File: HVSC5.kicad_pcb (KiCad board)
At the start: 2 copper layers, 220 x 152 mm, 339 parts, among them J1 test, J10 CONN_01X03, J11 test, J12 test, J13 test, J14 test, J15 test, J16 test, J17 CONN_COAXIAL, J18 CONN_01X03, J19 CONN_01X03, J2 test, J20 CONN_01X08, J21 test, J22 test, J23 test, J24 test, J25 CONN_01X05, J26 test, J27 test, J3 test, J4 test, J5 CONN_01X05, J6 test, J7 CONN_01X05, J8 CONN_COAXIAL, J9 DB9_Female_MountingHoles, SW1 SW_Push, SW3 SW_DPDT_x2, U1 AD7175-8, U10 LT1118-5V, U11 FOD0721, U12 DPBW06, U13 LTC2644, U14 uA7805, U15 INA128, U16 XR2206, U17 TLP176A, U18 ANA4522, U19 AQV258, U2 ADR4520, U20 AQV258, U21 ANA4522, U3 ADR445, U4 74LS04, U5 dsPIC33EV256GM002, U6 SN75451, U7 MAX232, U8 HFBR-2412, U9 HFBR-1414, X1 P7002SCLRP, X2 P7002SCLRP, X3 P7002SCLRP, X4 P7002SCLRP, X5 P7002SCLRP, X6 P7002SCLRP, Y1 16M, Y2 8M

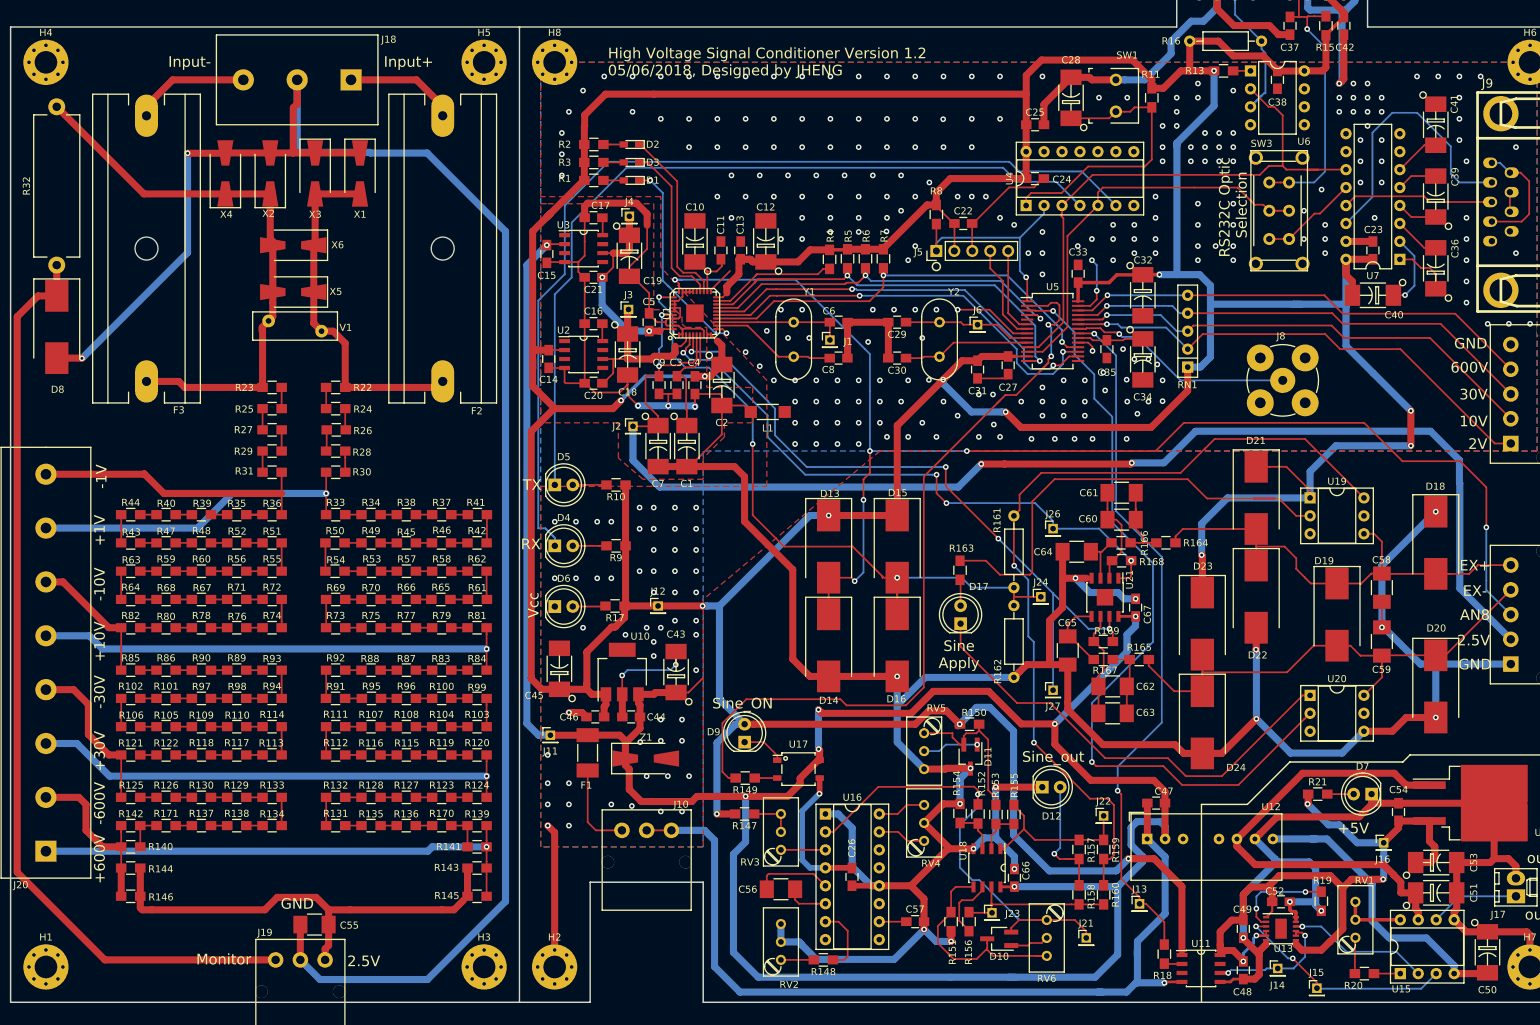
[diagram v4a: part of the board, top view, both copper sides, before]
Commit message: Selector Numbering
Selector numbering
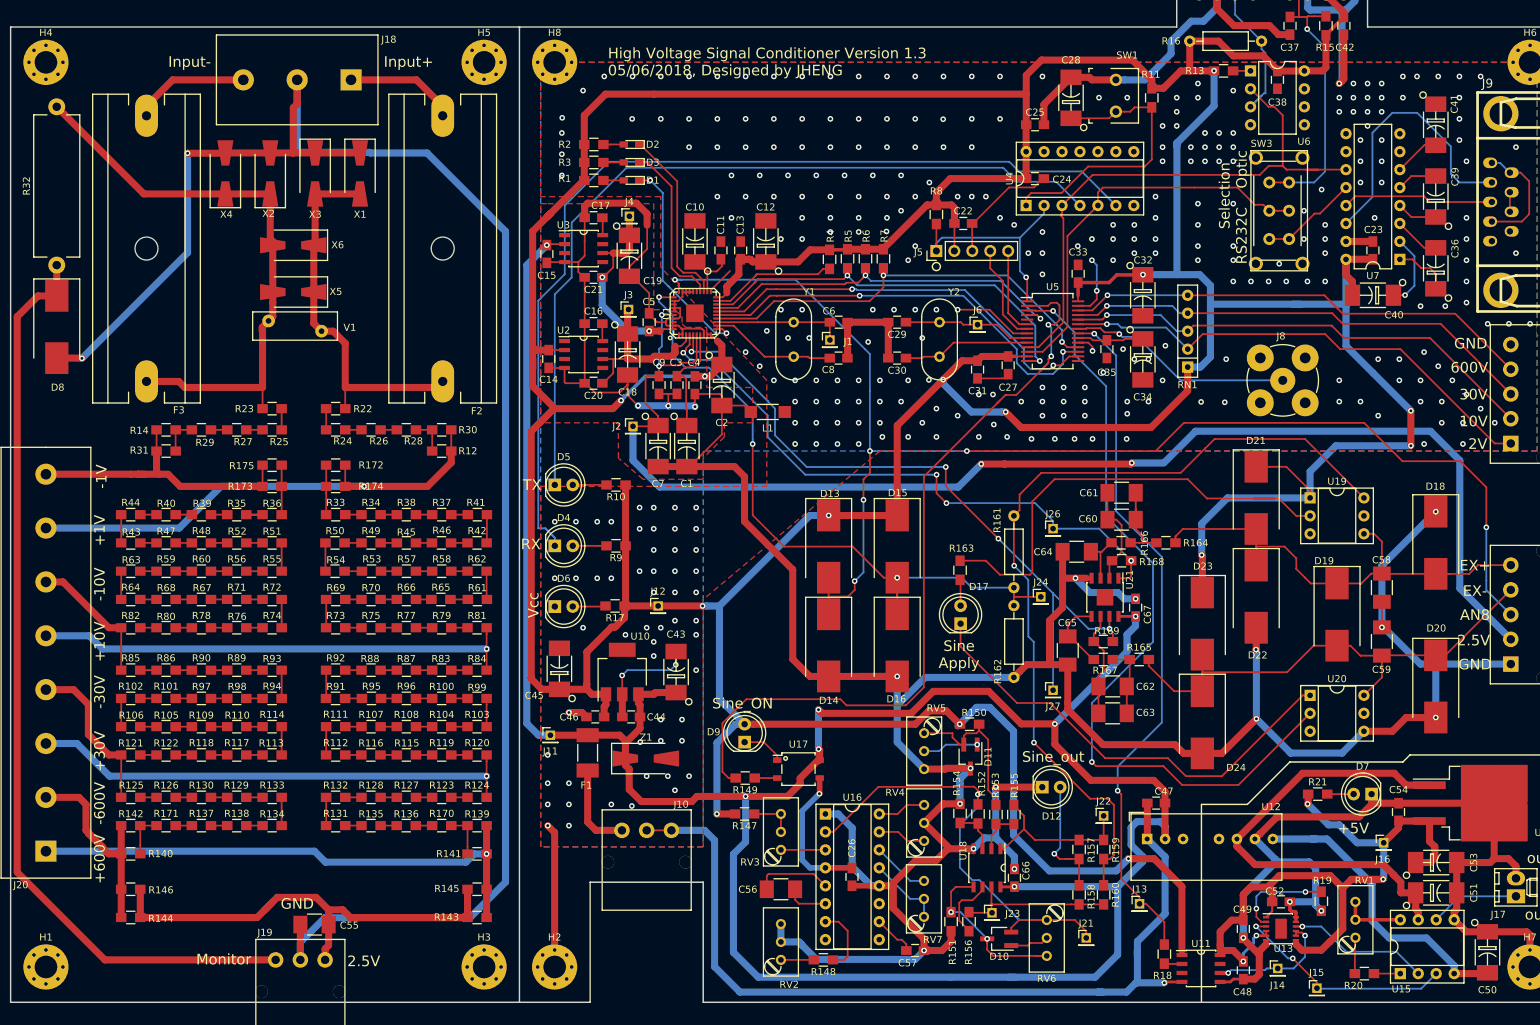
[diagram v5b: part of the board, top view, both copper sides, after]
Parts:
- added R12: 10k, Resistors_SMD:R_0805_HandSoldering, F.Cu at (104.0, 83.0)
- added R14: 10k, Resistors_SMD:R_0805_HandSoldering, F.Cu at (65.0, 80.0)
- added R172: 10k, Resistors_SMD:R_0805_HandSoldering, F.Cu at (89.0, 85.0)
- added R173: 10k, Resistors_SMD:R_0805_HandSoldering, F.Cu at (80.0, 88.0)
- added R174: 10k, Resistors_SMD:R_0805_HandSoldering, F.Cu at (89.0, 88.0)
- added R175: 10k, Resistors_SMD:R_0805_HandSoldering, F.Cu at (80.0, 85.0)
- added RV7: 500, Potentiometers:Potentiometer_Trimmer_Bourns_3296W, F.Cu at (172.2, 148.9)
- moved R30 16.2 mm to (104.0, 80.0), turned to 0 degrees
- moved R31 15.3 mm to (65.0, 83.0), turned to 180 degrees
- moved R28 10.4 mm to (99.0, 80.0)
- moved R29 10.4 mm to (70.0, 80.0)
- moved R143 7.00 mm to (109.0, 149.0)
- moved R144 7.00 mm to (60.0, 149.0)
- moved R27 5.00 mm to (75.0, 80.0), turned to 180 degrees
- moved R26 4.93 mm to (94.0, 80.0), turned to 0 degrees
- moved C57 4.08 mm to (171.0, 153.7)
- moved R22 3.00 mm to (89.0, 77.0)
- moved R23 3.00 mm to (80.0, 77.0)
- moved R24 3.00 mm to (89.0, 80.0)
- moved R25 3.00 mm to (80.0, 80.0)
- moved R140 1.00 mm to (60.0, 140.0)
- moved R141 1.00 mm to (109.0, 140.0)
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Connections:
- R33 pad 1: /Passive_Network/P1V -> Net-(R172-Pad2)
- R36 pad 1: /Passive_Network/N1V -> Net-(R173-Pad2)
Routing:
- net /Passive_Network/P1V: track 47.7 -> 71.5 mm
- net Net-(RV7-Pad1): track 0.00 -> 10.7 mm
- net /Passive_Network/P600V: track 72.6 -> 81.4 mm
- net Net-(RV7-Pad3): track 0.00 -> 8.15 mm
- net Net-(D10-Pad3): track 32.1 -> 24.7 mm, vias 0 -> 2
- net GNDREF: track 825.2 -> 818.0 mm, vias 20 -> 19
- net Net-(R173-Pad2): track 0.00 -> 7.10 mm
- net Net-(R172-Pad2): track 0.00 -> 7.00 mm
- net /Passive_Network/N600V: track 25.7 -> 32.0 mm
- net +12V: track 363.5 -> 358.8 mm
- net Net-(F1-Pad2): track 11.9 -> 15.6 mm
- net Net-(F3-Pad1): track 88.6 -> 91.6 mm
- net Net-(F2-Pad1): track 50.8 -> 53.8 mm
- net Net-(R14-Pad1): track 3.00 -> 5.30 mm
- net Net-(R12-Pad1): track 3.00 -> 5.30 mm
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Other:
- net class Power: clearance 0.2 -> 0.25
- board text added: "High Voltage Signal Conditioner Version 1.3 05/06/2018, Designed by JHENG"
- board text added: "Selection RS232C Optic"
- board text removed: "High Voltage Signal Conditioner Version 1.2 05/06/2018, Designed by JHENG"
- board text removed: "RS232C Optic Selection"

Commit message: 0805_넓히기
기타 수정
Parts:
- removed D15, D16: ES3J, Diodes_SMD:D_SMC_Handsoldering
- added C68: 20uF, Capacitors_SMD:C_1210_HandSoldering, F.Cu at (170.2, 98.0)
- added C69: 20uF, Capacitors_SMD:C_1210_HandSoldering, F.Cu at (166.6, 98.0)
- added C70: 20uF, Capacitors_SMD:C_1210_HandSoldering, F.Cu at (153.9, 96.0)
- added C71: 20uF, Capacitors_SMD:C_1210_HandSoldering, F.Cu at (170.2, 105.2)
- added C72: 20uF, Capacitors_SMD:C_1210_HandSoldering, F.Cu at (166.6, 105.2)
- added C73: 20uF, Capacitors_SMD:C_1210_HandSoldering, F.Cu at (153.9, 105.2)
- added C74: 0.1uF, Capacitors_SMD:C_0805_HandSoldering, F.Cu at (163.6, 103.6)
- added J28: test, Pin_Headers:Pin_Header_Straight_1x01_Pitch2.00mm, F.Cu at (162.6, 90.4)
- added J29: test, Pin_Headers:Pin_Header_Straight_1x01_Pitch2.00mm, F.Cu at (150.4, 90.4)
- added R176: 250, Resistors_SMD:R_0805_HandSoldering, F.Cu at (166.1, 93.7)
- added R177: 250, Resistors_SMD:R_0805_HandSoldering, F.Cu at (161.0, 93.7)
- added R178: 500, Resistors_SMD:R_0805_HandSoldering, F.Cu at (161.0, 96.3)
- added R179: 250, Resistors_SMD:R_0805_HandSoldering, F.Cu at (163.6, 110.2)
- added R180: 250, Resistors_SMD:R_0805_HandSoldering, F.Cu at (158.5, 110.2)
- added R181: 500, Resistors_SMD:R_0805_HandSoldering, F.Cu at (158.5, 107.7)
- added U22: ANA4522, USER:SOIC-8_3.9x4.9mm_Pitch1.27mm, F.Cu at (159.8, 102.6)
- D13, D14, D21, D22, D23, D24: footprint Diodes_SMD:D_SMC_Handsoldering -> USER:D_SMC_Handsoldering
- R100, R101, R102, R103, R104, R105, R106, R107, R108, R109, R110, R111, R112, R113, R114, R115, R116, R117, R118, R119, R12, R120, R121, R122, R123, R124, R125, R126, R127, R128, R129, R130, R131, R132, R133, R134, R135, R136, R137, R138, R139, R140, R141, R142, R143, R144, R145, R146, R170, R171, R172, R173, R174, R175, R22, R23, R24, R25, R26, R27, R28, R29, R30, R31, R33, R34, R35, R36, R37, R38, R39, R40, R41, R42, R43, R44, R45, R46, R47, R48, R49, R50, R51, R52, R53, R54, R55, R56, R57, R58, R59, R60, R61, R62, R63, R64, R65, R66, R67, R68, R69, R70, R71, R72, R73, R74, R75, R76, R77, R78, R79, R80, R81, R82, R83, R84, R85, R86, R87, R88, R89, R90, R91, R92, R93, R94, R95, R96, R97, R98, R99: footprint Resistors_SMD:R_0805_HandSoldering -> USER:R_0805_HandSoldering_long
- RV1: value 200 -> 2k
- U10: footprint TO_SOT_Packages_SMD:SOT-223 -> USER:SOT-223_LT1118
- U21: footprint Housings_SOIC:SOIC-8-1EP_3.9x4.9mm_Pitch1.27mm -> USER:SOIC-8_3.9x4.9mm_Pitch1.27mm
- U6: value SN75451 -> SN75452
- moved D14 97.1 mm to (255.3, 120.7), turned to 180 degrees
- moved D13 96.7 mm to (255.3, 90.4), turned to 0 degrees
- moved D6 32.2 mm to (120.0, 137.2)
- moved R17 27.1 mm to (120.7, 130.8), turned to 270 degrees
- moved J12 12.6 mm to (143.3, 114.0)
- moved C46 4.47 mm to (124.5, 116.3), turned to 90 degrees
- moved J26 2.11 mm to (192.0, 92.5)
- moved D18 0.81 mm to (243.8, 96.0)
- moved D20 0.81 mm to (243.8, 116.3)
- moved D23 0.43 mm to (211.5, 107.0)
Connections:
- C60 pad 1: Net-(C60-Pad1) -> /ADC7175/AIN2
- C61 pad 1: Net-(C60-Pad1) -> /ADC7175/AIN2
- C62 pad 1: Net-(C62-Pad1) -> /ADC7175/AIN3
- C63 pad 1: Net-(C62-Pad1) -> /ADC7175/AIN3
- D13 pad 2: /ADC7175/AIN8 -> /Voltage_Divider/Monitor
- D14 pad 1: /ADC7175/AIN8 -> /Voltage_Divider/Monitor
- J24 pad 1: /ADC7175/AIN9 -> Net-(J24-Pad1)
- J25 pad 3: /ADC7175/AIN8 -> /Voltage_Divider/Monitor
- R161 pad 1: /ADC7175/AIN9 -> Net-(J24-Pad1)
- R162 pad 2: /ADC7175/AIN9 -> Net-(J24-Pad1)
- R168 pad 2: Net-(C60-Pad1) -> Net-(R168-Pad2)
- R169 pad 2: Net-(C62-Pad1) -> Net-(R169-Pad2)
- SW3 pad 0: (no net) -> GND
- U21 pad 2: Net-(C60-Pad1) -> Net-(R168-Pad2)
- U21 pad 6: Net-(C62-Pad1) -> Net-(R169-Pad2)
- U4 pad 3: /dSPIC33EV/TXD -> Net-(U4-Pad3)
- U4 pad 5: /dSPIC33EV/RXD -> Net-(U4-Pad5)
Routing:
- net /Voltage_Divider/Monitor: track 0.00 -> 148.0 mm, vias 0 -> 2
- net /ADC7175/AIN8: track 190.9 -> 78.3 mm, vias 6 -> 2
- net GNDREF: track 818.0 -> 852.2 mm, vias 19 -> 21
- net Net-(J24-Pad1): track 0.00 -> 28.6 mm, vias 0 -> 1
- net /ADC7175/AIN9: track 94.4 -> 77.5 mm
- net +12V: track 358.8 -> 375.6 mm, vias 7 -> 8
- net VCC: track 888.0 -> 904.4 mm, vias 14 -> 16
- net GND: track 325.2 -> 308.8 mm, vias 336 -> 417
- net Net-(C62-Pad1): track 15.1 -> 0.00 mm
- net Net-(C60-Pad1): track 14.4 -> 0.00 mm
- net Net-(C70-Pad1): track 0.00 -> 12.2 mm
- net Net-(C71-Pad2): track 0.00 -> 12.1 mm
- net /ADC7175/AIN3: track 99.2 -> 110.7 mm
- net Net-(C73-Pad1): track 0.00 -> 10.3 mm
- net Net-(C68-Pad2): track 0.00 -> 9.90 mm
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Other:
- board text added: "12V GND"

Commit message: 1206 update
다시 보세요.
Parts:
- R100, R101, R102, R103, R104, R105, R106, R107, R108, R109, R110, R111, R112, R113, R114, R115, R116, R117, R118, R119, R12, R120, R121, R122, R123, R124, R125, R126, R127, R128, R129, R130, R131, R132, R133, R134, R135, R136, R137, R138, R139, R140, R141, R142, R143, R144, R145, R146, R170, R171, R172, R173, R174, R175, R22, R23, R24, R25, R26, R27, R28, R29, R30, R31, R33, R34, R35, R36, R37, R38, R39, R40, R41, R42, R43, R44, R45, R46, R47, R48, R49, R50, R51, R52, R53, R54, R55, R56, R57, R58, R59, R60, R61, R62, R63, R64, R65, R66, R67, R68, R69, R70, R71, R72, R73, R74, R75, R76, R77, R78, R79, R80, R81, R82, R83, R84, R85, R86, R87, R88, R89, R90, R91, R92, R93, R94, R95, R96, R97, R98, R99: footprint USER:R_0805_HandSoldering_long -> Resistors_SMD:R_1206_HandSoldering
- moved J20 13.0 mm to (35.0, 132.0)
- moved R12 3.00 mm to (107.0, 83.0)
- moved R30 3.00 mm to (107.0, 80.0)
- moved R28 2.00 mm to (101.0, 80.0)
- moved R26 1.00 mm to (95.0, 80.0)

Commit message: 2차PCB
U22 포함
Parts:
- D1, D2, D3: footprint LEDs:LED_0603_HandSoldering -> LEDs:LED_0805_HandSoldering
- R14: footprint Resistors_SMD:R_0805_HandSoldering -> Resistors_SMD:R_1206_HandSoldering
- moved H1 20.0 mm to (28.0, 156.0)
- moved H4 20.0 mm to (28.0, 28.0)
- moved R102 19.0 mm to (41.0, 118.0)
- moved R106 19.0 mm to (41.0, 122.0)
- moved R121 19.0 mm to (41.0, 126.0)
- moved R125 19.0 mm to (41.0, 132.0)
- moved R140 19.0 mm to (41.0, 140.0)
- moved R142 19.0 mm to (41.0, 136.0)
- moved R144 19.0 mm to (41.0, 149.0)
- moved R146 19.0 mm to (41.0, 145.0)
- moved R43 19.0 mm to (41.0, 96.0)
- moved R44 19.0 mm to (41.0, 92.0)
- moved R63 19.0 mm to (41.0, 100.0)
- moved R64 19.0 mm to (41.0, 104.0)
- moved R82 19.0 mm to (41.0, 108.0)
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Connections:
- H1 pad 1: GND -> Net-(H1-Pad1)
- H3 pad 1: GND -> Net-(H3-Pad1)
- H4 pad 1: GND -> Net-(H4-Pad1)
- H5 pad 1: GND -> Net-(H5-Pad1)
- U4 pad 3: Net-(U4-Pad3) -> /dSPIC33EV/TXD
- U4 pad 5: Net-(U4-Pad5) -> /dSPIC33EV/RXD
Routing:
- net /Passive_Network/P10V: track 69.1 -> 91.0 mm
- net /Passive_Network/P30V: track 70.3 -> 92.1 mm
- net /Passive_Network/P600V: track 81.4 -> 97.7 mm
- net GNDREF: track 852.2 -> 835.9 mm, vias 21 -> 20
- net +2V5: track 255.6 -> 270.4 mm
- net /Passive_Network/Monitor: track 131.5 -> 145.9 mm
- net /Passive_Network/P1V: track 71.5 -> 84.0 mm
- net Net-(F2-Pad2): track 15.9 -> 22.3 mm
- net Net-(F3-Pad1): track 91.6 -> 97.8 mm
- net Net-(F3-Pad2): track 16.6 -> 22.3 mm
- net Net-(F2-Pad1): track 53.8 -> 59.5 mm
- net /Passive_Network/N600V: track 32.0 -> 27.3 mm
- net /Voltage_Divider/Wire_Break: track 115.0 -> 110.9 mm
- net Net-(R61-Pad2): track 2.46 -> 6.27 mm
- net /Passive_Network/N1V: track 42.7 -> 45.9 mm
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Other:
- board size 220 x 152 mm -> 240 x 152 mm
- net class Power: clearance 0.25 -> 0.2
- board text added: "High Voltage Signal Conditioner Version 1.3 18/06/2018, Designed by JHENG"
- board text removed: "High Voltage Signal Conditioner Version 1.3 05/06/2018, Designed by JHENG"
